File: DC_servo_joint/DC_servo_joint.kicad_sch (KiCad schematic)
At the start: 52 parts, among them U1 AS5600, U2 ESP32-C3-WROOM-02, U3 SP3485EN, U5 TPS563200

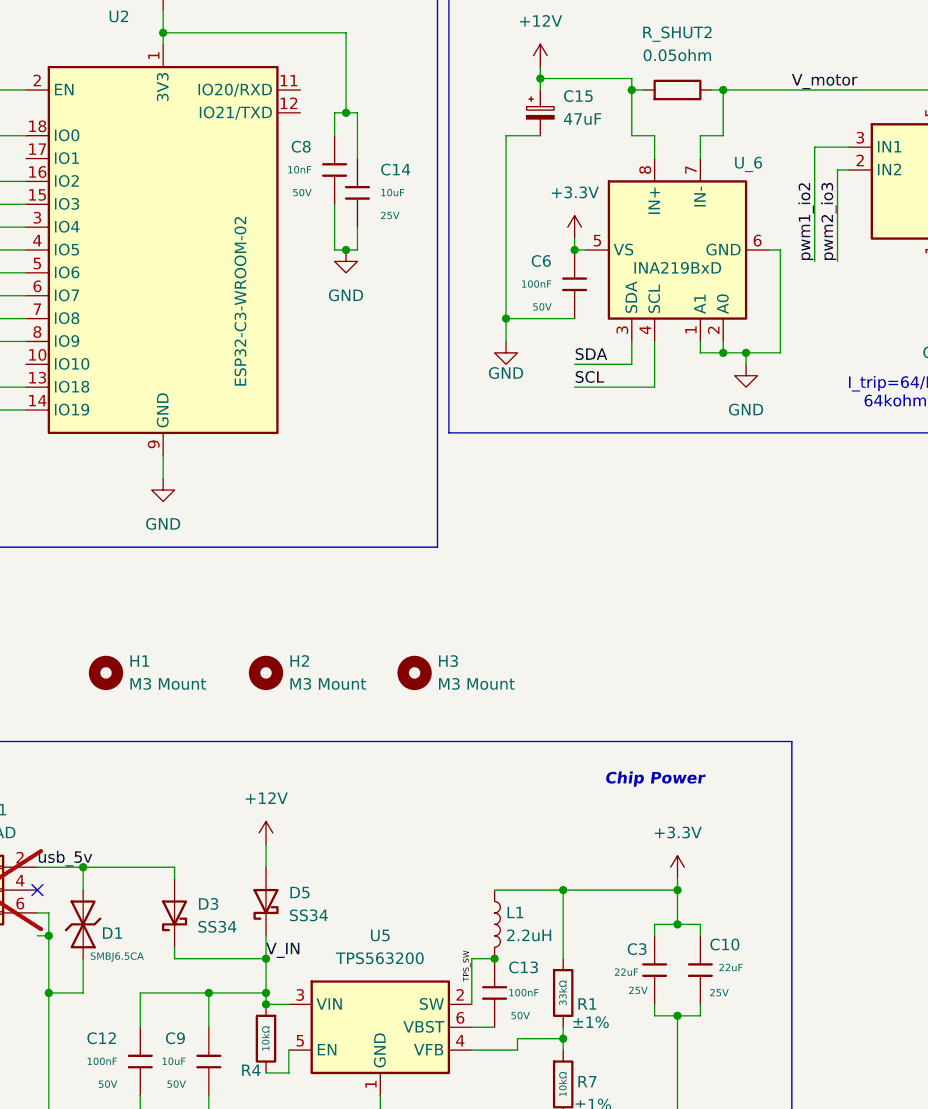
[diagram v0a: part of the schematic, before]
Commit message: Fixed the via size issue. Replace the INA219 with proper part
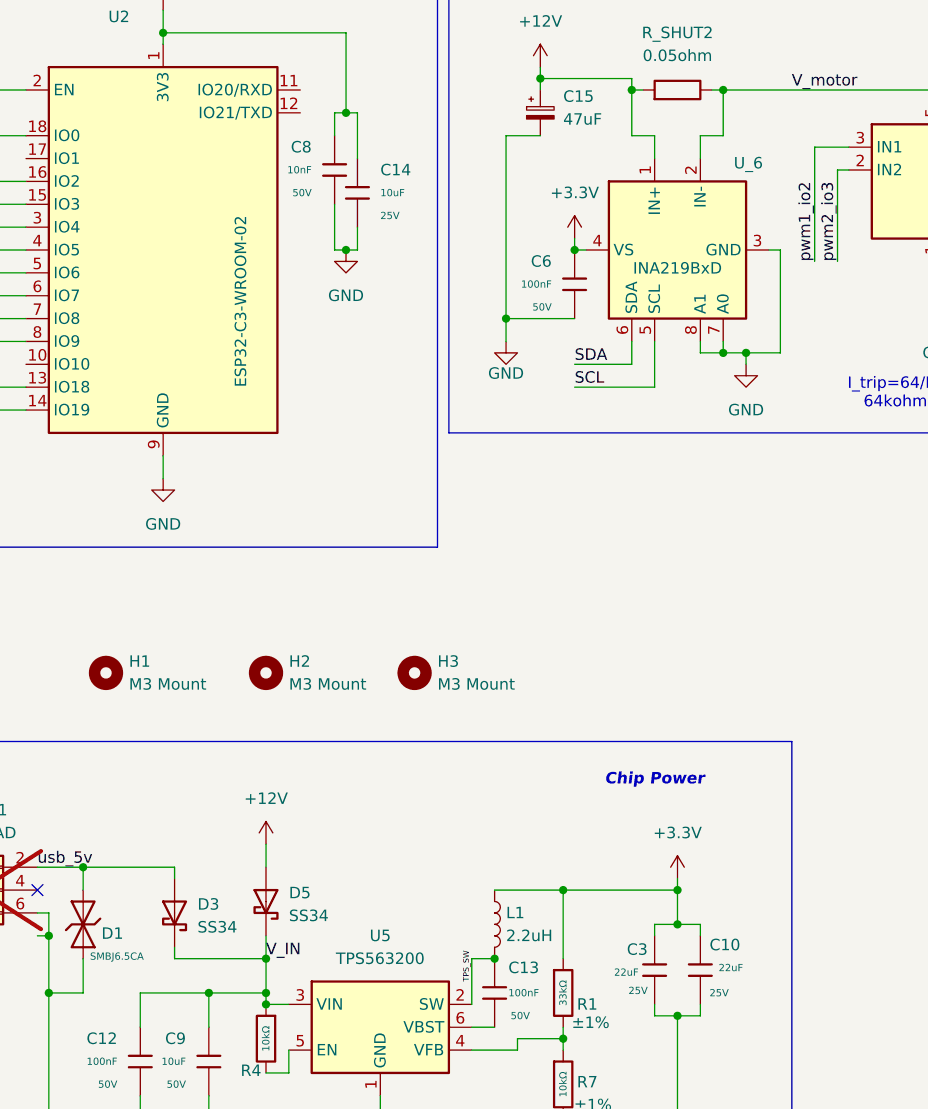
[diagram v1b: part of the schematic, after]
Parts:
- D3, D5: footprint Diode_SMD:D_SMA -> PCM_JLCPCB:D_SMA; symbol Diode:SS34 -> PCM_JLCPCB-Diodes:Schottky,SS34; Attrition Qty (none) -> 8; Category (none) -> Diodes,Schottky Barrier Diodes (SBD); Class (none) -> Basic Component; Diode Configuration (none) -> Independent Type; Forward Voltage (Vf@If) (none) -> 550mV@3A; LCSC (none) -> C8678; Manufacturer (none) -> MDD（Microdiode Electronics）; Minimum Qty (none) -> 5; Part (none) -> SS34; Price (none) -> 0.030USD; Process (none) -> SMT; Rectified Current (none) -> 3A; Reverse Leakage Current (Ir) (none) -> 500uA@40V; Reverse Voltage (Vr) (none) -> 40V; Stock (none) -> 1971586
- U_6: footprint Package_SO:SOIC-8_3.9x4.9mm_P1.27mm -> Package_TO_SOT_SMD:SOT-23-8; symbol Sensor_Energy:INA219BxD -> Sensor_Energy:INA219AxDCN
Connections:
- net +12V: now also U_6.1 (IN+); no longer U_6.8 (IN+)
- net +3.3V: now also U_6.4 (VS); no longer U_6.5 (VS)
- net GND: now also U_6.3 (GND), U_6.7 (A0), U_6.8 (A1); no longer U_6.1 (A1), U_6.2 (A0), U_6.6 (GND)
- net SCL: now also U_6.5 (SCL); no longer U_6.4 (SCL)
- net SDA: now also U_6.6 (SDA); no longer U_6.3 (SDA)
- net V_motor: now also U_6.2 (IN-); no longer U_6.7 (IN-)

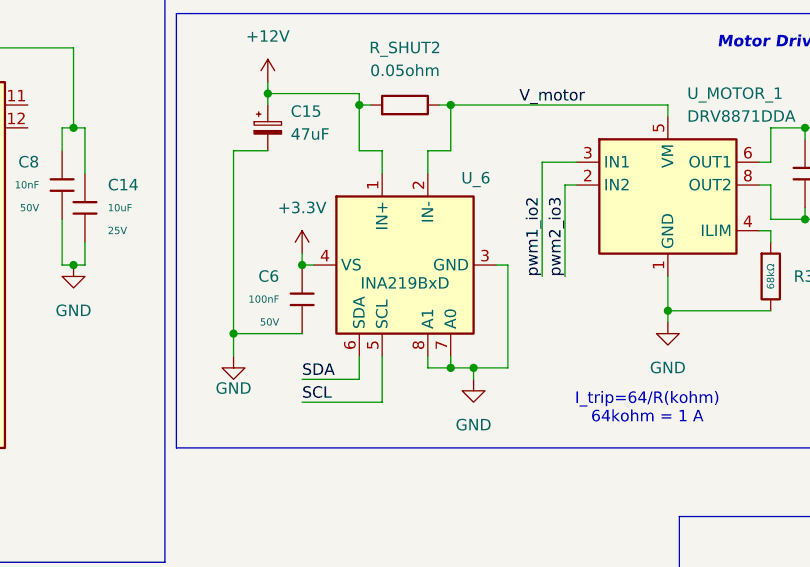
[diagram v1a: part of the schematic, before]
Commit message: Updated the proper value for INA219AxD and did part selection on JLC plugin
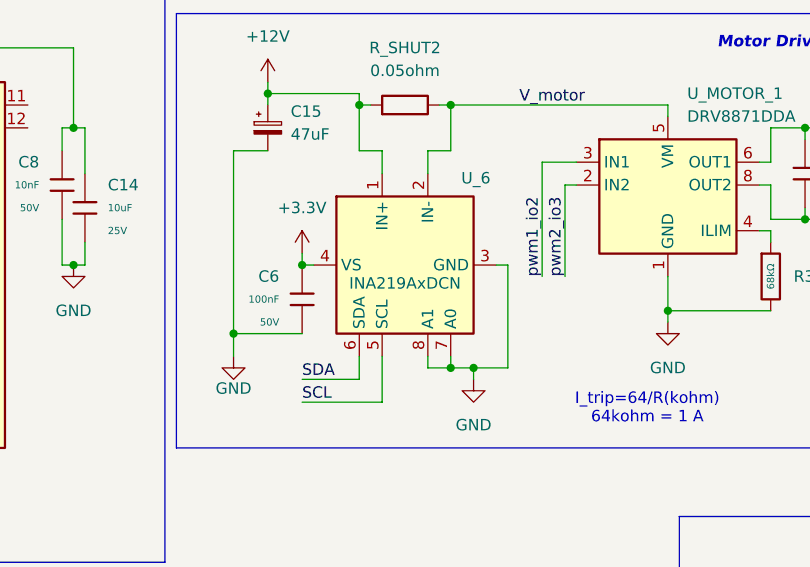
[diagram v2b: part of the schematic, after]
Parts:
- U_6: value INA219BxD -> INA219AxDCN
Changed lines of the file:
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@@
 			)
 		)
-		(property "Value" "INA219BxD"
+		(property "Value" "INA219AxDCN"
 			(at 199.39 56.642 90)
 			(effects
